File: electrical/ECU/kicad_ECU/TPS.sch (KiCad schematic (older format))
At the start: 3 parts

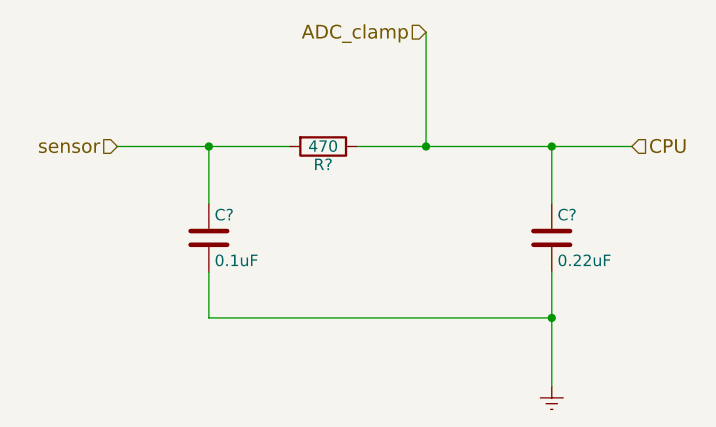
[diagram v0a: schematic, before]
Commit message: fixed some naming errors and initial round of double checking
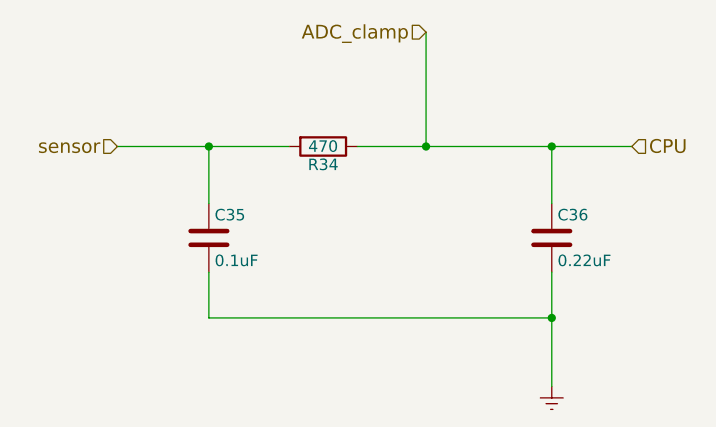
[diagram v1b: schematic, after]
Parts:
- gave numbers to parts that had none: 3
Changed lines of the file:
@@
 $Descr A4 11693 8268
 encoding utf-8
-Sheet 12 33
+Sheet 16 33
 Title "Throttle Position Sensor"
 Date ""
@@
 CPU
 $Comp
-L R R?
+L R R33
 U 1 1 597755F5
 P 5700 3150
-AR Path="/5974D512/5977551F/597755F5" Ref="R?"  Part="1"
-AR Path="/5974D512/59775648/597755F5" Ref="R?"  Part="1"
-F 0 "R?" V 5780 3150 50  0000 C CNN
+AR Path="/5974D512/5977551F/597755F5" Ref="R33"  Part="1"
+AR Path="/5974D512/59775648/597755F5" Ref="R34"  Part="1"
+F 0 "R34" V 5780 3150 50  0000 C CNN
 F 1 "470" V 5700 3150 50  0000 C CNN
 F 2 "" V 5630 3150 50  0001 C CNN
@@
 $EndComp
 $Comp
-L C C?
+L C C33
 U 1 1 597755FC
 P 5200 3550
-AR Path="/5974D512/5977551F/597755FC" Ref="C?"  Part="1"
-AR Path="/5974D512/59775648/597755FC" Ref="C?"  Part="1"
-F 0 "C?" H 5225 3650 50  0000 L CNN
+AR Path="/5974D512/5977551F/597755FC" Ref="C33"  Part="1"
+AR Path="/5974D512/59775648/597755FC" Ref="C35"  Part="1"
+F 0 "C35" H 5225 3650 50  0000 L CNN
 F 1 "0.1uF" H 5225 3450 50  0000 L CNN
 F 2 "" H 5238 3400 50  0001 C CNN
@@
 $EndComp
 $Comp
-L C C?
+L C C34
 U 1 1 59775603
 P 6700 3550
-AR Path="/5974D512/5977551F/59775603" Ref="C?"  Part="1"
-AR Path="/5974D512/59775648/59775603" Ref="C?"  Part="1"
-F 0 "C?" H 6725 3650 50  0000 L CNN
+AR Path="/5974D512/5977551F/59775603" Ref="C34"  Part="1"
+AR Path="/5974D512/59775648/59775603" Ref="C36"  Part="1"
+F 0 "C36" H 6725 3650 50  0000 L CNN
 F 1 "0.22uF" H 6725 3450 50  0000 L CNN
 F 2 "" H 6738 3400 50  0001 C CNN
@@
 $EndComp
 $Comp
-L Earth #PWR?
+L Earth #PWR43
 U 1 1 5977560A
 P 6700 4200
-AR Path="/5974D512/5977551F/5977560A" Ref="#PWR?"  Part="1"
-AR Path="/5974D512/59775648/5977560A" Ref="#PWR?"  Part="1"
-F 0 "#PWR?" H 6700 3950 50  0001 C CNN
+AR Path="/5974D512/5977551F/5977560A" Ref="#PWR43"  Part="1"
+AR Path="/5974D512/59775648/5977560A" Ref="#PWR44"  Part="1"
+F 0 "#PWR44" H 6700 3950 50  0001 C CNN
 F 1 "Earth" H 6700 4050 50  0001 C CNN
 F 2 "" H 6700 4200 50  0001 C CNN
